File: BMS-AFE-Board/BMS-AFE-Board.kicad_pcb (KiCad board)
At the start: 2 copper layers, 20.4 x 66.3 mm, 6 parts, among them J1 Conn_01x10, J2 Conn_01x10, J3 Conn_01x15, J4 Conn_01x15, U1 BQ76920PW, U2 BQ76930DBT

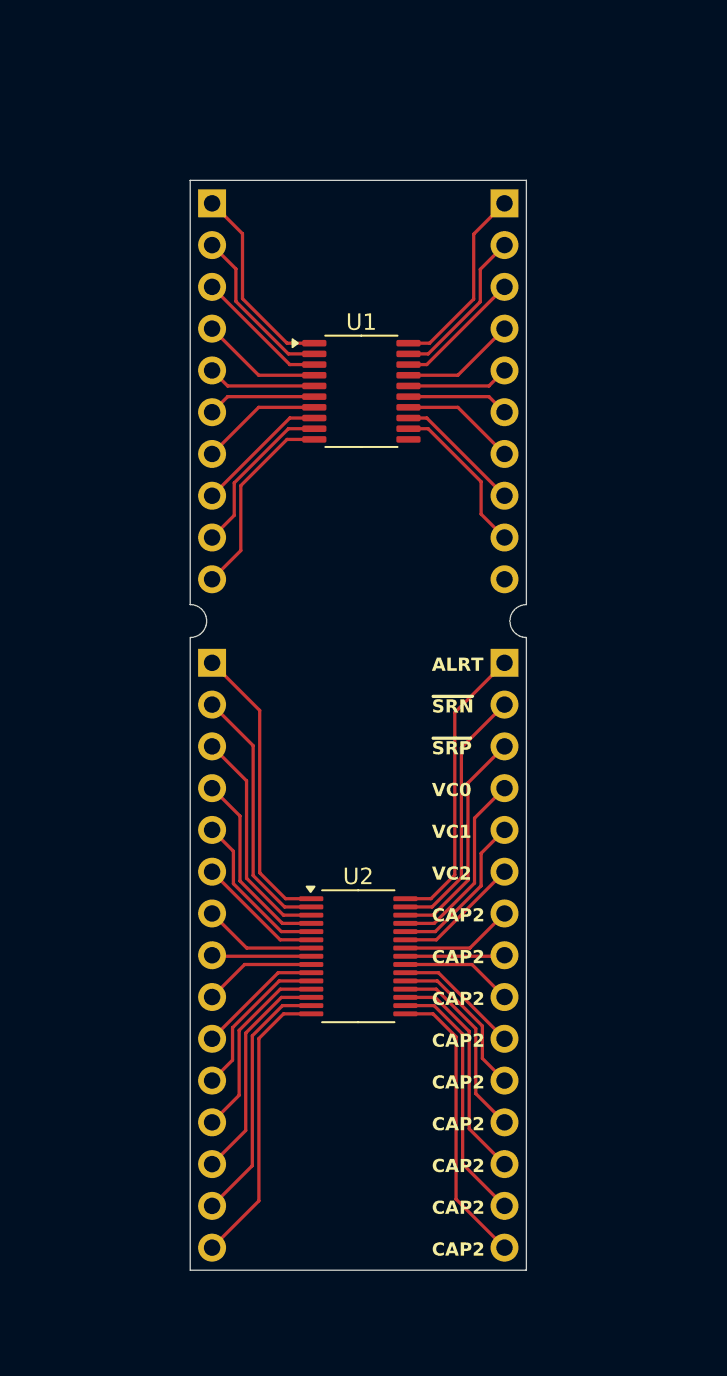
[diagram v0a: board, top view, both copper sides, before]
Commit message: Finished tracks, ground via left
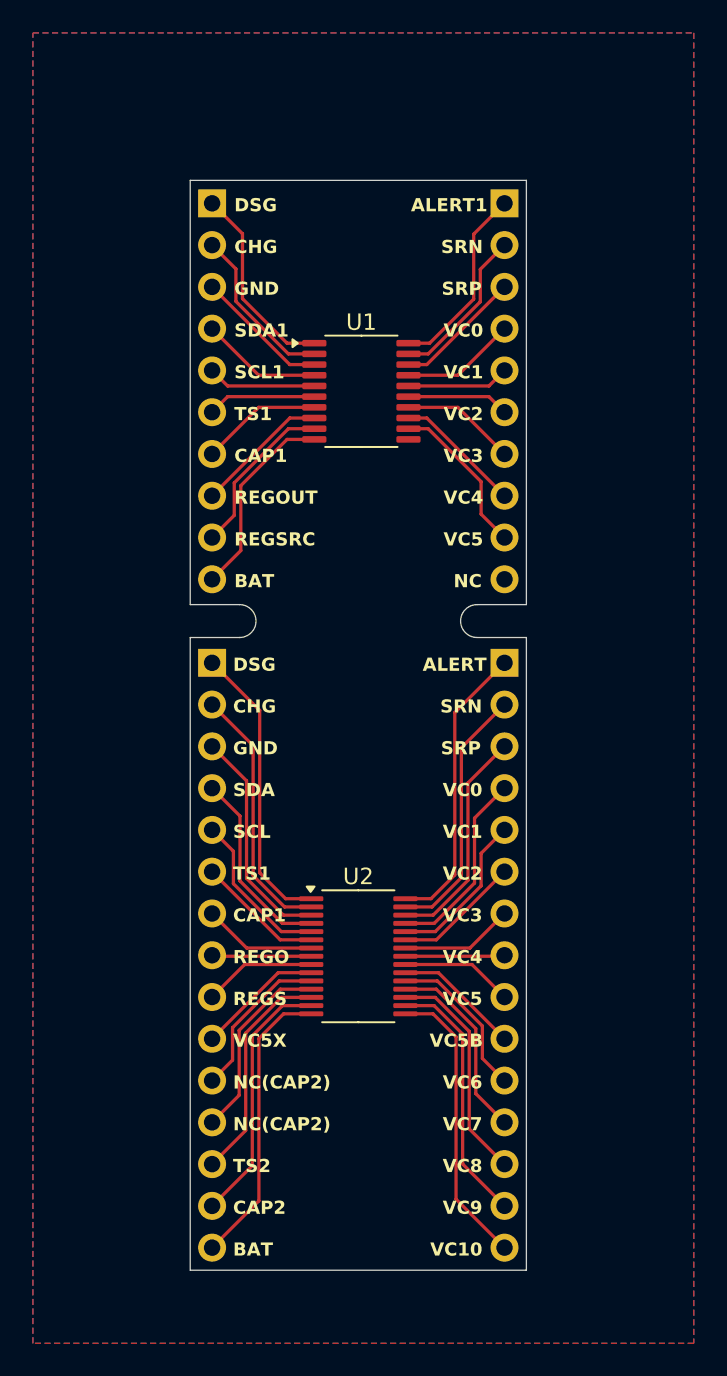
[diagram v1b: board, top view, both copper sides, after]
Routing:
- added copper zone on B.Cu, net GND
- added copper zone on F.Cu, net GND
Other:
- outline, holes or cut-outs redrawn
- board text added: "ALERT"
- board text added: "ALERT1"
- board text added: "BAT"
- board text added: "CAP1"
- board text added: "CHG"
- board text added: "DSG"
- board text added: "GND"
- board text added: "NC"
- board text added: "NC(CAP2)"
- board text added: "REGO"
- board text added: "REGOUT"
- board text added: "REGS"
- board text added: "REGSRC"
- board text added: "SCL"
- board text added: "SCL1"
- board text added: "SDA"
- board text added: "SDA1"
- board text added: "SRN"
- board text added: "SRP"
- board text added: "TS1"
- board text added: "TS2"
- board text added: "VC10"
- board text added: "VC3"
- board text added: "VC4"
- board text added: "VC5"
- board text added: "VC5B"
- board text added: "VC5X"
- board text added: "VC6"
- board text added: "VC7"
- board text added: "VC8"
- board text added: "VC9"
- board text removed: "ALRT"
- board text removed: "~{SRN}"
- board text removed: "~{SRP}"
